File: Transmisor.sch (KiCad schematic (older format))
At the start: 26 parts

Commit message: Prueba despues del error de MEGAsync
Este commit hay que hacerle un rebase
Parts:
- gave numbers to parts that had none: 26
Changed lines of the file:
@@
 $EndDescr
 $Comp
-L GND #PWR?
+L GND #PWR8
 U 1 1 59D03B24
 P 3450 3150
-F 0 "#PWR?" H 3450 2900 50  0001 C CNN
+F 0 "#PWR8" H 3450 2900 50  0001 C CNN
 F 1 "GND" H 3450 3000 50  0000 C CNN
 F 2 "" H 3450 3150 50  0001 C CNN
@@
 $EndComp
 $Comp
-L Jumper_NC_Dual JP?
+L Jumper_NC_Dual JP1
 U 1 1 59D03B67
 P 3450 2100
-F 0 "JP?" H 3500 2000 50  0000 L CNN
+F 0 "JP1" H 3500 2000 50  0000 L CNN
 F 1 "Jumper_NC_Dual" H 3450 2200 50  0000 C BNN
 F 2 "" H 3450 2100 50  0001 C CNN
@@
 $EndComp
 $Comp
-L +3.3V #PWR?
+L +3.3V #PWR11
 U 1 1 59D03BAE
 P 3850 2000
-F 0 "#PWR?" H 3850 1850 50  0001 C CNN
+F 0 "#PWR11" H 3850 1850 50  0001 C CNN
 F 1 "+3.3V" H 3850 2140 50  0000 C CNN
 F 2 "" H 3850 2000 50  0001 C CNN
@@
 $EndComp
 $Comp
-L GND #PWR?
+L GND #PWR7
 U 1 1 59D03BCA
 P 3100 2200
-F 0 "#PWR?" H 3100 1950 50  0001 C CNN
+F 0 "#PWR7" H 3100 1950 50  0001 C CNN
 F 1 "GND" H 3100 2050 50  0000 C CNN
 F 2 "" H 3100 2200 50  0001 C CNN
@@
 $EndComp
 $Comp
-L R R?
+L R R3
 U 1 1 59D03BE8
 P 3450 2500
-F 0 "R?" V 3530 2500 50  0000 C CNN
+F 0 "R3" V 3530 2500 50  0000 C CNN
 F 1 "3K3" V 3450 2500 50  0000 C CNN
 F 2 "" V 3380 2500 50  0001 C CNN
@@
 $EndComp
 $Comp
-L C C?
+L C C7
 U 1 1 59D03FCB
 P 3900 2850
-F 0 "C?" H 3925 2950 50  0000 L CNN
+F 0 "C7" H 3925 2950 50  0000 L CNN
 F 1 "1nF" H 3925 2750 50  0000 L CNN
 F 2 "" H 3938 2700 50  0001 C CNN
@@
 $EndComp
 $Comp
-L GND #PWR?
+L GND #PWR9
 U 1 1 59D0403F
 P 3600 2850
-F 0 "#PWR?" H 3600 2600 50  0001 C CNN
+F 0 "#PWR9" H 3600 2600 50  0001 C CNN
 F 1 "GND" H 3600 2700 50  0000 C CNN
 F 2 "" H 3600 2850 50  0001 C CNN
@@
 $EndComp
 $Comp
-L R R?
+L R R6
 U 1 1 59D040A8
 P 4050 2400
-F 0 "R?" V 4130 2400 50  0000 C CNN
+F 0 "R6" V 4130 2400 50  0000 C CNN
 F 1 "3K3" V 4050 2400 50  0000 C CNN
 F 2 "" V 3980 2400 50  0001 C CNN
@@
 $EndComp
 $Comp
-L GND #PWR?
+L GND #PWR14
 U 1 1 59D04624
 P 5100 4700
-F 0 "#PWR?" H 5100 4450 50  0001 C CNN
+F 0 "#PWR14" H 5100 4450 50  0001 C CNN
 F 1 "GND" H 5100 4550 50  0000 C CNN
 F 2 "" H 5100 4700 50  0001 C CNN
@@
 $EndComp
 $Comp
-L Crystal Y?
+L Crystal Y1
 U 1 1 59D04800
 P 4600 4900
-F 0 "Y?" H 4600 5050 50  0000 C CNN
+F 0 "Y1" H 4600 5050 50  0000 C CNN
 F 1 "27.12 MHz" H 4600 4750 50  0000 C CNN
 F 2 "" H 4600 4900 50  0001 C CNN
@@
 $EndComp
 $Comp
-L C C?
+L C C8
 U 1 1 59D04855
 P 4350 5250
-F 0 "C?" H 4375 5350 50  0000 L CNN
+F 0 "C8" H 4375 5350 50  0000 L CNN
 F 1 "10pF" H 4375 5150 50  0000 L CNN
 F 2 "" H 4388 5100 50  0001 C CNN
@@
 $EndComp
 $Comp
-L C C?
+L C C9
 U 1 1 59D0496A
 P 4850 5250
-F 0 "C?" H 4875 5350 50  0000 L CNN
+F 0 "C9" H 4875 5350 50  0000 L CNN
 F 1 "10pF" H 4650 5150 50  0000 L CNN
 F 2 "" H 4888 5100 50  0001 C CNN
@@
 $EndComp
 $Comp
-L GND #PWR?
+L GND #PWR12
 U 1 1 59D04B81
 P 4600 5500
-F 0 "#PWR?" H 4600 5250 50  0001 C CNN
+F 0 "#PWR12" H 4600 5250 50  0001 C CNN
 F 1 "GND" H 4600 5350 50  0000 C CNN
 F 2 "" H 4600 5500 50  0001 C CNN
@@
 $EndComp
 $Comp
-L R R?
+L R R5
 U 1 1 59D04EC6
 P 3900 4300
-F 0 "R?" V 3980 4300 50  0000 C CNN
+F 0 "R5" V 3980 4300 50  0000 C CNN
 F 1 "3K3" V 3900 4300 50  0000 C CNN
 F 2 "" V 3830 4300 50  0001 C CNN
@@
 $EndComp
 $Comp
-L R R?
+L R R4
 U 1 1 59D04FA0
 P 3700 4300
-F 0 "R?" V 3780 4300 50  0000 C CNN
+F 0 "R4" V 3780 4300 50  0000 C CNN
 F 1 "3K3" V 3700 4300 50  0000 C CNN
 F 2 "" V 3630 4300 50  0001 C CNN
@@
 $EndComp
 $Comp
-L GND #PWR?
+L GND #PWR10
 U 1 1 59D05040
 P 3800 4550
-F 0 "#PWR?" H 3800 4300 50  0001 C CNN
+F 0 "#PWR10" H 3800 4300 50  0001 C CNN
 F 1 "GND" H 3800 4400 50  0000 C CNN
 F 2 "" H 3800 4550 50  0001 C CNN
@@
 CR95_RX
 $Comp
-L GND #PWR?
+L GND #PWR16
 U 1 1 59D05394
 P 5700 4500
-F 0 "#PWR?" H 5700 4250 50  0001 C CNN
+F 0 "#PWR16" H 5700 4250 50  0001 C CNN
 F 1 "GND" H 5700 4350 50  0000 C CNN
 F 2 "" H 5700 4500 50  0001 C CNN
@@
 SPI_MISO
 $Comp
-L L_Core_Ferrite L?
+L L_Core_Ferrite L5
 U 1 1 59D061B1
 P 6100 2950
-F 0 "L?" V 6050 2950 50  0000 C CNN
+F 0 "L5" V 6050 2950 50  0000 C CNN
 F 1 "742792042" V 6210 2950 50  0000 C CNN
 F 2 "" H 6100 2950 50  0001 C CNN
@@
 $EndComp
 $Comp
-L L_Core_Ferrite L?
+L L_Core_Ferrite L4
 U 1 1 59D062AB
 P 6100 2700
-F 0 "L?" V 6050 2700 50  0000 C CNN
+F 0 "L4" V 6050 2700 50  0000 C CNN
 F 1 "742792042" V 6210 2700 50  0000 C CNN
 F 2 "" H 6100 2700 50  0001 C CNN
@@
 $EndComp
 $Comp
-L CR95HF U?
+L CR95HF U1
 U 1 1 59D0664E
 P 4900 3400
-F 0 "U?" H 4350 4400 50  0000 C CNN
+F 0 "U1" H 4350 4400 50  0000 C CNN
 F 1 "CR95HF" H 4450 4350 50  0000 C CNN
 F 2 "" H 4700 3750 50  0001 C CNN
@@
 $EndComp
 $Comp
-L C C?
+L C C11
 U 1 1 59D06901
 P 6650 3050
-F 0 "C?" H 6675 3150 50  0000 L CNN
+F 0 "C11" H 6675 3150 50  0000 L CNN
 F 1 "220pF" H 6675 2950 50  0000 L CNN
 F 2 "" H 6688 2900 50  0001 C CNN
@@
 $EndComp
 $Comp
-L C C?
+L C C13
 U 1 1 59D06941
 P 7050 3050
-F 0 "C?" H 7075 3150 50  0000 L CNN
+F 0 "C13" H 7075 3150 50  0000 L CNN
 F 1 "OPEN" H 7075 2950 50  0000 L CNN
 F 2 "" H 7088 2900 50  0001 C CNN
@@
 $EndComp
 $Comp
-L C C?
+L C C10
 U 1 1 59D06AB7
 P 6650 2650
-F 0 "C?" H 6675 2750 50  0000 L CNN
+F 0 "C10" H 6675 2750 50  0000 L CNN
 F 1 "220pF" H 6675 2550 50  0000 L CNN
 F 2 "" H 6688 2500 50  0001 C CNN
@@
 $EndComp
 $Comp
-L C C?
+L C C12
 U 1 1 59D06ABD
 P 7050 2650
-F 0 "C?" H 7075 2750 50  0000 L CNN
+F 0 "C12" H 7075 2750 50  0000 L CNN
 F 1 "OPEN" H 7075 2550 50  0000 L CNN
 F 2 "" H 7088 2500 50  0001 C CNN
@@
 $EndComp
 $Comp
-L GND #PWR?
+L GND #PWR17
 U 1 1 59D06E6F
 P 7350 2900
-F 0 "#PWR?" H 7350 2650 50  0001 C CNN
+F 0 "#PWR17" H 7350 2650 50  0001 C CNN
 F 1 "GND" H 7350 2750 50  0000 C CNN
 F 2 "" H 7350 2900 50  0001 C CNN
@@
 $EndComp
 $Comp
-L C C?
+L C C15
 U 1 1 59D07384
 P 7750 2450
-F 0 "C?" H 7775 2550 50  0000 L CNN
+F 0 "C15" H 7775 2550 50  0000 L CNN
 F 1 "56pF" H 7775 2350 50  0000 L CNN
 F 2 "" H 7788 2300 50  0001 C CNN
@@
 $EndComp
 $Comp
-L C C?
+L C C16
 U 1 1 59D073DB
 P 7750 3250
-F 0 "C?" H 7775 3350 50  0000 L CNN
+F 0 "C16" H 7775 3350 50  0000 L CNN
 F 1 "56pF" H 7775 3150 50  0000 L CNN
 F 2 "" H 7788 3100 50  0001 C CNN
@@
 Connection ~ 7050 3250
 $Comp
-L C C?
+L C C14
 U 1 1 59D075BB
 P 7750 2150
-F 0 "C?" H 7775 2250 50  0000 L CNN
+F 0 "C14" H 7775 2250 50  0000 L CNN
 F 1 "OPEN" H 7775 2050 50  0000 L CNN
 F 2 "" H 7788 2000 50  0001 C CNN
@@
 $EndComp
 $Comp
-L C C?
+L C C17
 U 1 1 59D07626
 P 7750 3550
-F 0 "C?" H 7775 3650 50  0000 L CNN
+F 0 "C17" H 7775 3650 50  0000 L CNN
 F 1 "OPEN" H 7775 3450 50  0000 L CNN
 F 2 "" H 7788 3400 50  0001 C CNN
@@
 	7950 2150 7900 2150
 $Comp
-L C C?
+L C C18
 U 1 1 59D0798E
 P 8150 2850
-F 0 "C?" H 8175 2950 50  0000 L CNN
+F 0 "C18" H 8175 2950 50  0000 L CNN
 F 1 "150pF" H 8175 2750 50  0000 L CNN
 F 2 "" H 8188 2700 50  0001 C CNN
@@
 Connection ~ 8000 3250
 $Comp
-L R R?
+L R R7
 U 1 1 59D07BEE
 P 7050 1800
-F 0 "R?" V 7130 1800 50  0000 C CNN
+F 0 "R7" V 7130 1800 50  0000 C CNN
 F 1 "330" V 7050 1800 50  0000 C CNN
 F 2 "" V 6980 1800 50  0001 C CNN
@@
 $EndComp
 $Comp
-L R R?
+L R R8
 U 1 1 59D07F23
 P 7050 3900
-F 0 "R?" V 7130 3900 50  0000 C CNN
+F 0 "R8" V 7130 3900 50  0000 C CNN
 F 1 "330" V 7050 3900 50  0000 C CNN
 F 2 "" V 6980 3900 50  0001 C CNN
@@
 Connection ~ 8150 2450
 $Comp
-L C C?
+L C C19
 U 1 1 59D098E2
 P 8500 2850
-F 0 "C?" H 8525 2950 50  0000 L CNN
+F 0 "C19" H 8525 2950 50  0000 L CNN
 F 1 "150pF" H 8525 2750 50  0000 L CNN
 F 2 "" H 8538 2700 50  0001 C CNN
@@
 	8500 3250 8500 3000
 $Comp
-L R R?
+L R R9
 U 1 1 59D09A70
 P 8800 2850
-F 0 "R?" V 8880 2850 50  0000 C CNN
+F 0 "R9" V 8880 2850 50  0000 C CNN
 F 1 "OPEN" V 8800 2850 50  0000 C CNN
 F 2 "" V 8730 2850 50  0001 C CNN
@@
 Connection ~ 8500 3250
 $Comp
-L Antenna_Loop AE?
+L Antenna_Loop AE1
 U 1 1 59D09C83
 P 9300 2750
-F 0 "AE?" H 9350 2750 50  0000 C CNN
+F 0 "AE1" H 9350 2750 50  0000 C CNN
 F 1 "Antenna_Loop" H 9350 2950 50  0000 C CNN
 F 2 "" H 9300 2750 50  0001 C CNN
@@
 Connection ~ 8800 3250
 $Comp
-L VPS_MAIN #PWR?
+L VPS_MAIN #PWR13
 U 1 1 59D0A388
 P 4650 1950
-F 0 "#PWR?" H 4850 2000 60  0001 C CNN
+F 0 "#PWR13" H 4850 2000 60  0001 C CNN
 F 1 "VPS_MAIN" H 4650 2100 60  0000 C CNN
 F 2 "" H 4650 1950 60  0001 C CNN
@@
 	4650 2200 4650 1950
 $Comp
-L VPS_TX #PWR?
+L VPS_TX #PWR15
 U 1 1 59D0A69D
 P 5150 1950
-F 0 "#PWR?" H 5350 2000 60  0001 C CNN
+F 0 "#PWR15" H 5350 2000 60  0001 C CNN
 F 1 "VPS_TX" H 5150 2100 60  0000 C CNN
 F 2 "" H 5150 1950 60  0001 C CNN

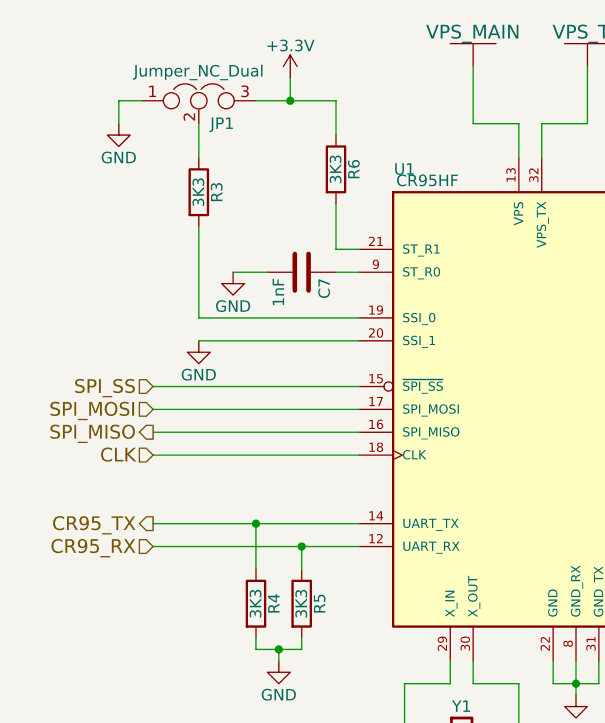
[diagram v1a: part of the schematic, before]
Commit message: Reestructuracion de esquematico
Entra todo en una sola pagina, por lo que no hice separacion jerarquica. Actualizados footprints y algunos campos para Kicost
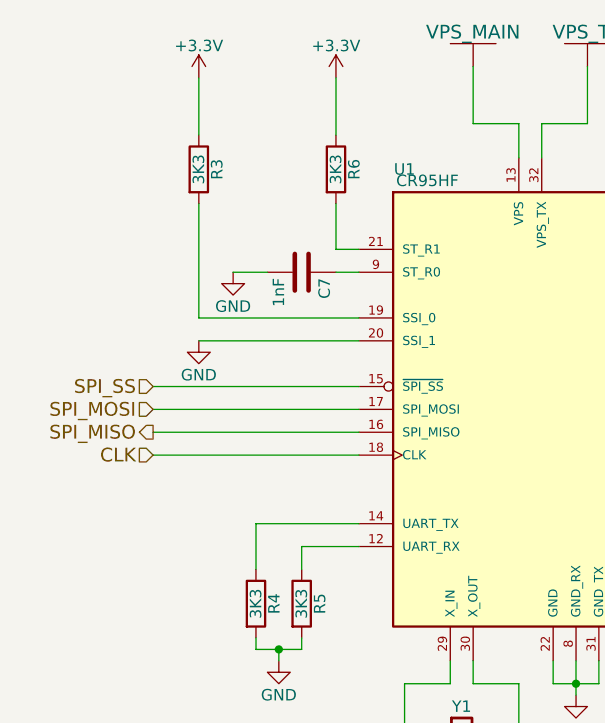
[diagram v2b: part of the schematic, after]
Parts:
- removed JP1: Jumper_NC_Dual, symbol Jumper_NC_Dual
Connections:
- net +3V3: now also R3.1
- net CR95_RX: no longer names the net of R5.1, U1.12 (UART_RX)
- net CR95_TX: no longer names the net of R4.1, U1.14 (UART_TX)
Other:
- moved on the sheet: R3
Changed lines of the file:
@@
-$EndComp
-$Comp
-L Jumper_NC_Dual JP1
-U 1 1 59D03B67
-P 3450 2100
-F 0 "JP1" H 3500 2000 50  0000 L CNN
-F 1 "Jumper_NC_Dual" H 3450 2200 50  0000 C BNN
-F 2 "" H 3450 2100 50  0001 C CNN
-F 3 "" H 3450 2100 50  0001 C CNN
-	1    3450 2100
-	1    0    0    -1
 $EndComp
 $Comp
 L +3.3V #PWR11
 U 1 1 59D03BAE
-P 3850 2000
-F 0 "#PWR11" H 3850 1850 50  0001 C CNN
-F 1 "+3.3V" H 3850 2140 50  0000 C CNN
-F 2 "" H 3850 2000 50  0001 C CNN
-F 3 "" H 3850 2000 50  0001 C CNN
-	1    3850 2000
-	1    0    0    -1
-$EndComp
-$Comp
-L GND #PWR7
-U 1 1 59D03BCA
-P 3100 2200
-F 0 "#PWR7" H 3100 1950 50  0001 C CNN
-F 1 "GND" H 3100 2050 50  0000 C CNN
-F 2 "" H 3100 2200 50  0001 C CNN
-F 3 "" H 3100 2200 50  0001 C CNN
-	1    3100 2200
+P 4050 2000
+F 0 "#PWR11" H 4050 1850 50  0001 C CNN
+F 1 "+3.3V" H 4050 2140 50  0000 C CNN
+F 2 "" H 4050 2000 50  0001 C CNN
+F 3 "" H 4050 2000 50  0001 C CNN
+	1    4050 2000
 	1    0    0    -1
 $EndComp
@@
 L R R3
 U 1 1 59D03BE8
-P 3450 2500
-F 0 "R3" V 3530 2500 50  0000 C CNN
-F 1 "3K3" V 3450 2500 50  0000 C CNN
-F 2 "" V 3380 2500 50  0001 C CNN
-F 3 "" H 3450 2500 50  0001 C CNN
-	1    3450 2500
+P 3450 2400
+F 0 "R3" V 3530 2400 50  0000 C CNN
+F 1 "3K3" V 3450 2400 50  0000 C CNN
+F 2 "" V 3380 2400 50  0001 C CNN
+F 3 "" H 3450 2400 50  0001 C CNN
+	1    3450 2400
 	1    0    0    -1
 $EndComp
@@
 	1    0    0    -1
 $EndComp
-Text HLabel 3250 3950 0    60   Output ~ 0
-CR95_TX
-Text HLabel 3250 4050 0    60   Input ~ 0
-CR95_RX
 $Comp
 L GND #PWR16
@@
 	4150 3150 3450 3150
 Wire Wire Line
-	3700 2100 4050 2100
-Wire Wire Line
-	3200 2100 3100 2100
-Wire Wire Line
-	3100 2100 3100 2200
-Wire Wire Line
-	3450 2200 3450 2350
-Wire Wire Line
-	3450 2650 3450 3050
+	3450 2550 3450 3050
 Wire Wire Line
 	3450 3050 4150 3050
@@
 	4050 2750 4050 2550
 Wire Wire Line
-	3850 2000 3850 2100
-Wire Wire Line
-	4050 2100 4050 2250
-Connection ~ 3850 2100
+	4050 2000 4050 2250
 Wire Wire Line
 	5000 4550 5000 4650
@@
 Connection ~ 4600 5450
 Wire Wire Line
-	3250 3950 4150 3950
-Wire Wire Line
 	3700 3950 3700 4150
-Wire Wire Line
-	3250 4050 4150 4050
 Wire Wire Line
 	3900 4050 3900 4150
@@
 	3800 4550 3800 4500
 Connection ~ 3800 4500
-Connection ~ 3700 3950
-Connection ~ 3900 4050
 Wire Wire Line
 	5700 3300 5700 4500
@@
 Wire Wire Line
 	4950 2200 4950 2350
+Wire Wire Line
+	4150 4050 3900 4050
+Wire Wire Line
+	3700 3950 4150 3950
+$Comp
+L +3.3V #PWR?
+U 1 1 59D180BD
+P 3450 2000
+F 0 "#PWR?" H 3450 1850 50  0001 C CNN
+F 1 "+3.3V" H 3450 2140 50  0000 C CNN
+F 2 "" H 3450 2000 50  0001 C CNN
+F 3 "" H 3450 2000 50  0001 C CNN
+	1    3450 2000
+	1    0    0    -1
+$EndComp
+Wire Wire Line
+	3450 2250 3450 2000
 $EndSCHEMATC
